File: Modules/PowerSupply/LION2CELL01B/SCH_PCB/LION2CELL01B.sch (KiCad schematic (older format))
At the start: 93 parts, among them J1 JUMP_4X2, J10 JUMP_2x1, J11 JUMP_2x1, J12 JUMP_2x1, J13 JUMP_4X2, J2 JUMP_2x1, J3 JUMP_2x1, J4 JUMP_2x1, J5 JUMP_2x1, J6 JUMP_2x1, J7 JUMP_4X2, J8 CONN1_1, J9 CONN1_1, P1 _, P2 _, P3 _, P4 _, Q1 IRLML6244, Q2 MMBF170LT1G, Q3 MMBF170LT1G, Q4 BSS83P, SW1 SW_PUSH, U1 BQ29209, U2 BQ24103, U3 BQ34Z100, U4 SN74HC164D

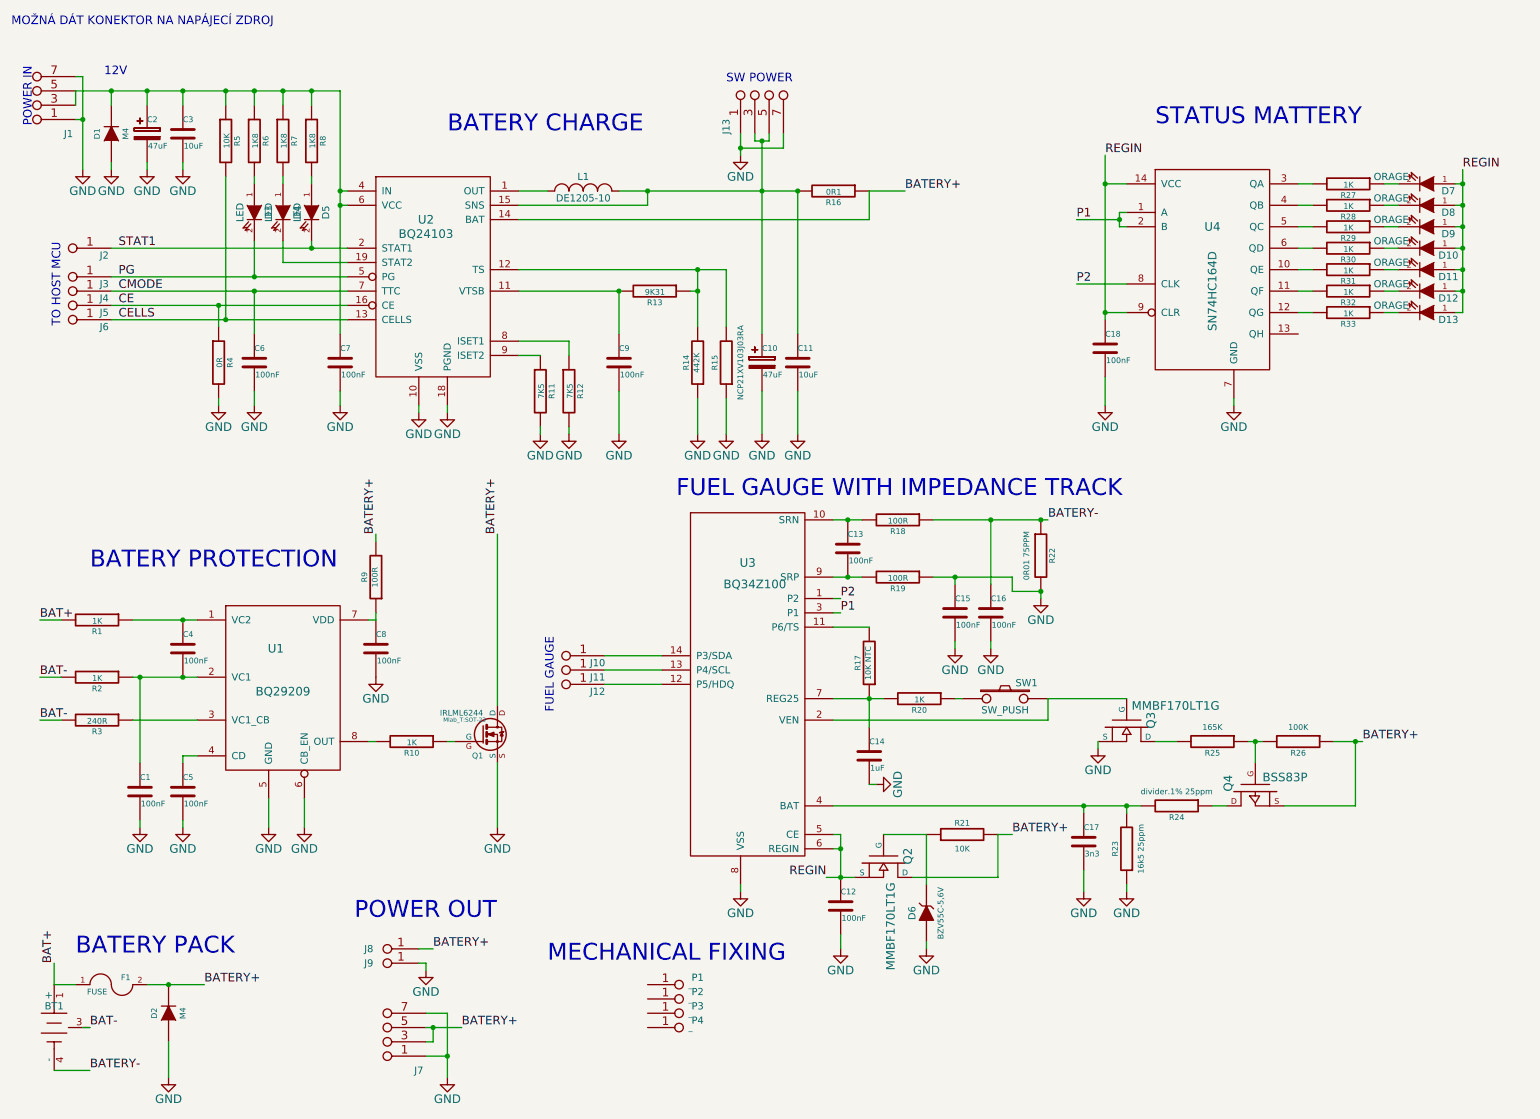
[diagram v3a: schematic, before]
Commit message: Uprava popisku a vedeni spoju ve schema.
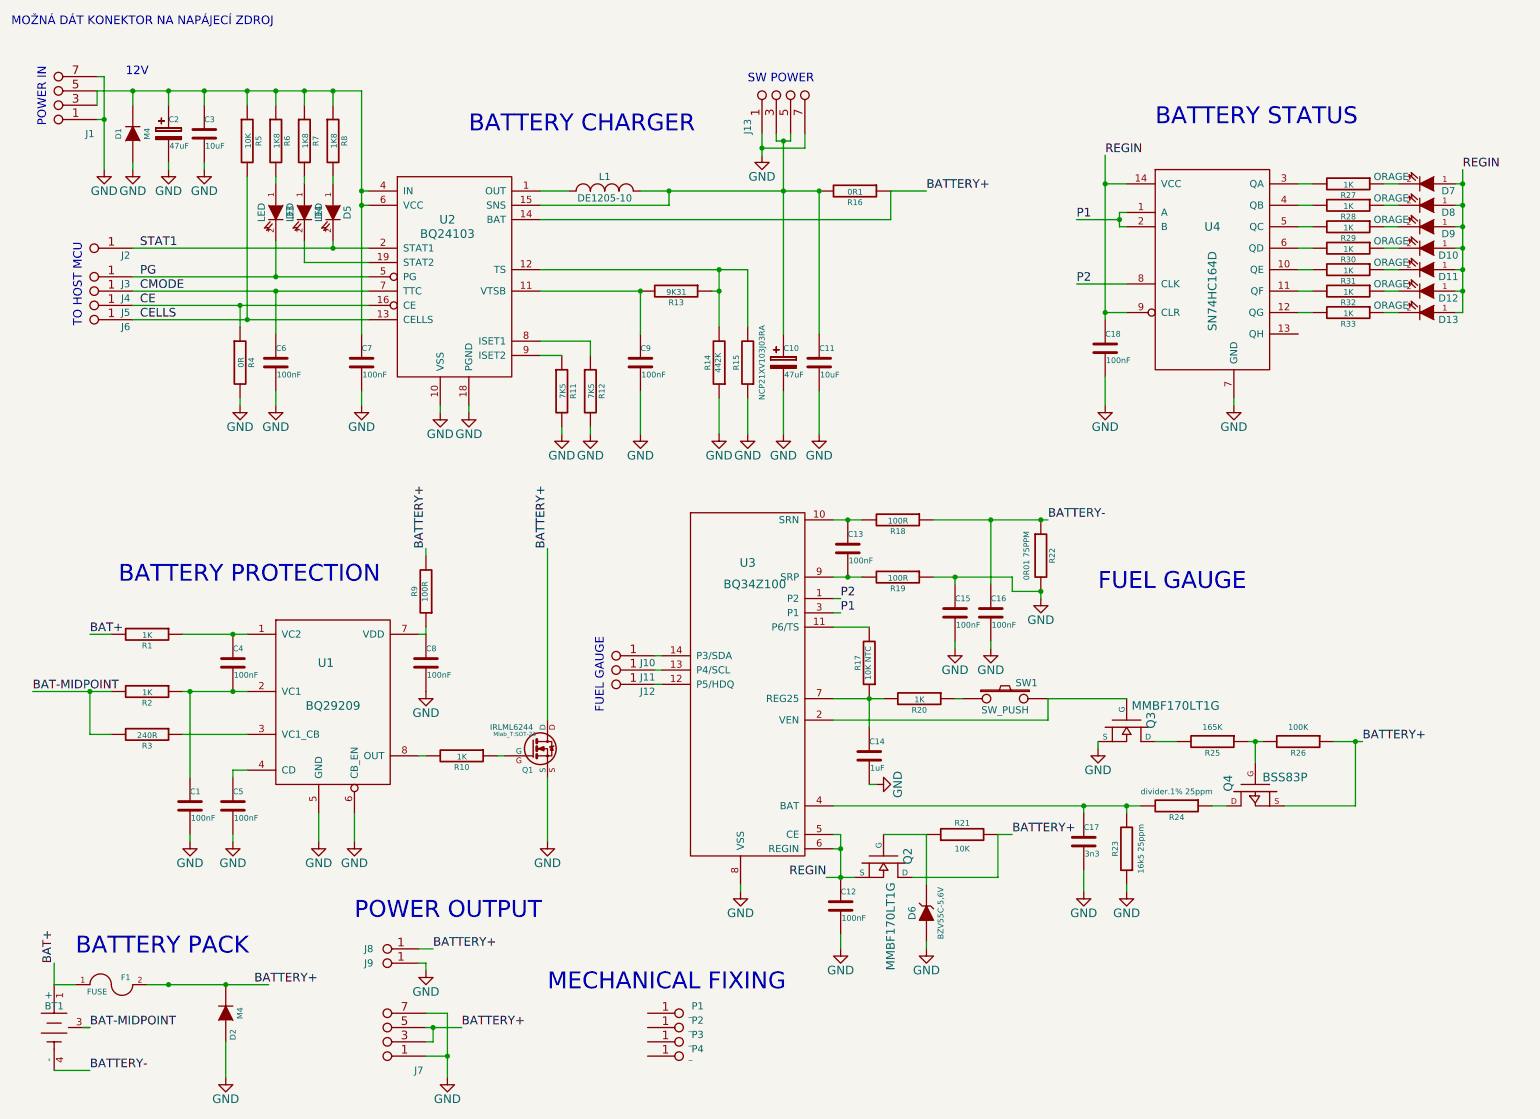
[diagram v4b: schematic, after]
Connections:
- net BAT- renamed BAT-MIDPOINT
- net BATERY+ renamed BATTERY+
- net BATERY- renamed BATTERY-
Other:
- note added: "BATTERY CHARGER"
- note added: "BATTERY PACK"
- note added: "BATTERY PROTECTION"
- note added: "BATTERY STATUS"
- note added: "POWER OUTPUT"
- note removed: "BATERY CHARGE"
- note removed: "BATERY PACK"
- note removed: "BATERY PROTECTION"
- note removed: "FUEL GAUGE WITH IMPEDANCE TRACK"
- note removed: "POWER OUT"
- note removed: "STATUS MATTERY"
- moved on the sheet: C1, C10, C11, C2, C3, C4, C5, C6, C7, C8, C9, D1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

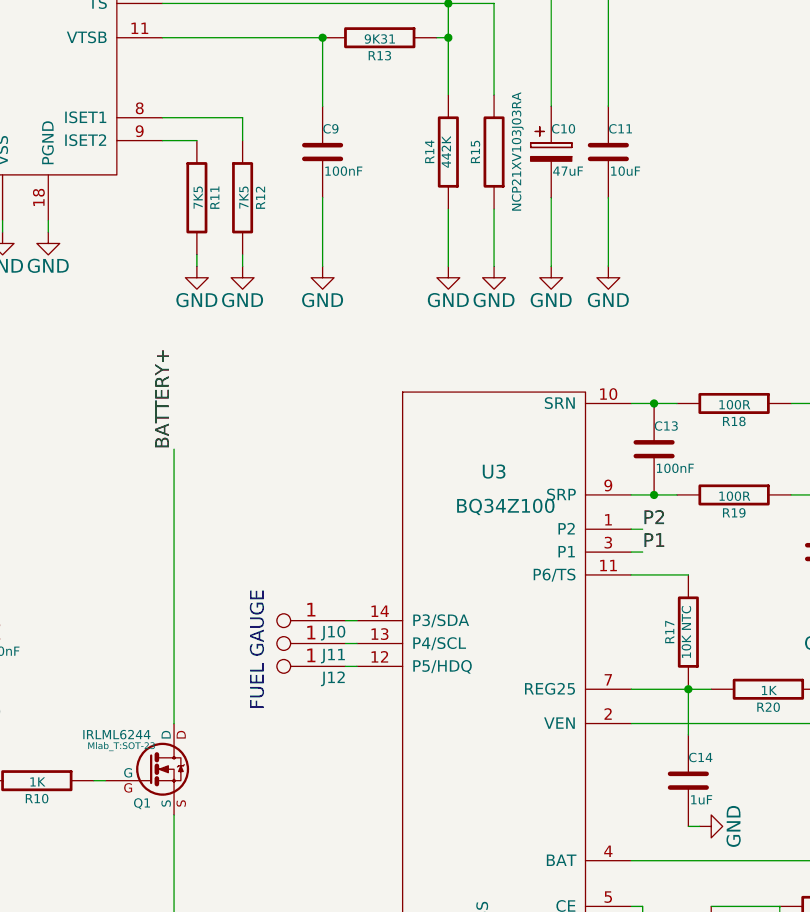
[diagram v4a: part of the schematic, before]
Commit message: 
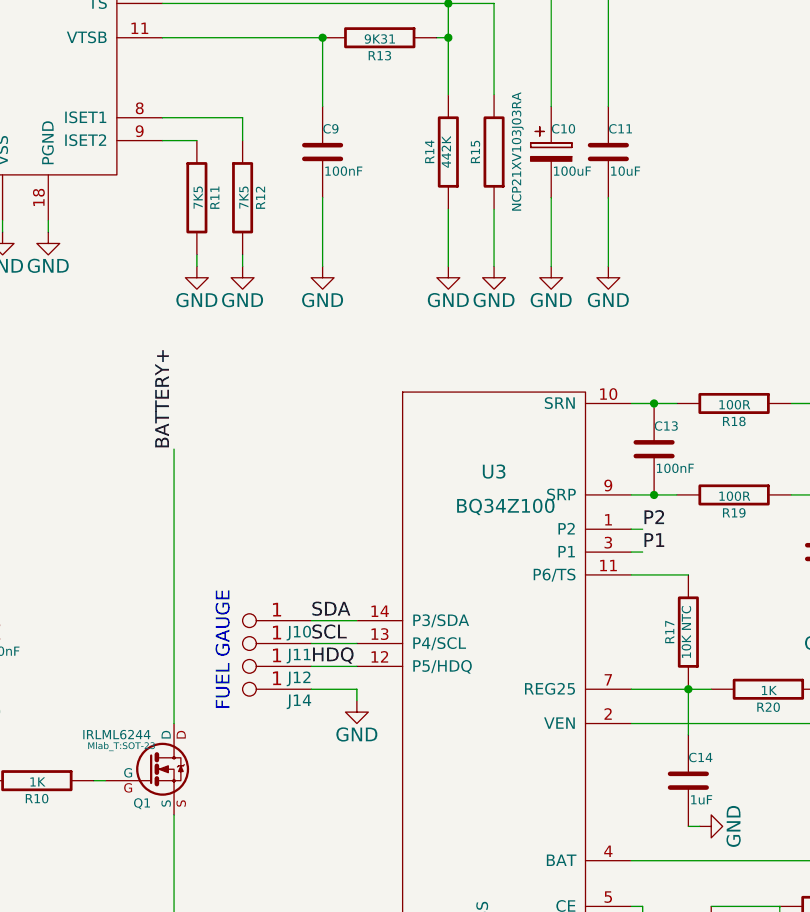
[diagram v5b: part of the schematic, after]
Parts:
- added J14: JUMP_2x1, Mlab_Pin_Headers:Straight_1x02, symbol JUMP_2x1
- C10: value 47uF -> 100uF; footprint Mlab_C:TantalC_SizeC_Reflow -> Mlab_C:TantalC_SizeD_Reflow
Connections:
- net GND: now also J14.1, J14.2 (1)
- net SDA: now reaches J10.1, J10.2 (1), U3.14 (P3/SDA)
- net HDQ: now reaches J12.1, J12.2 (1), U3.12 (P5/HDQ)
- net SCL: now reaches J11.1, J11.2 (1), U3.13 (P4/SCL)
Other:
- moved on the sheet: J10, J11, J12
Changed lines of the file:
@@
 LIBS:contrib
 LIBS:valves
+LIBS:ADC-DAC
+LIBS:asp-134604-01_(fmc)
+LIBS:clock
+LIBS:header
+LIBS:Jumpers
+LIBS:konektory
+LIBS:mechanical
+LIBS:MLAB_D
+LIBS:MLAB_IO
+LIBS:MLAB_Jumpers
+LIBS:OpAmp
+LIBS:sata7-67491-1030
+LIBS:MLAB_BATERY
+LIBS:MLAB_T
 LIBS:LION2CELL01B-cache
 EELAYER 25 0
@@
 L JUMP_2x1 J10
 U 1 1 5532725C
-P 4500 4500
-F 0 "J10" H 4150 4700 50  0000 C CNN
-F 1 "JUMP_2x1" V 4500 4650 40  0001 C CNN
-F 2 "Mlab_Pin_Headers:Straight_1x02" H 4500 4500 60  0001 C CNN
-F 3 "" H 4500 4500 60  0000 C CNN
-	1    4500 4500
+P 4350 4500
+F 0 "J10" H 4000 4700 50  0000 C CNN
+F 1 "JUMP_2x1" V 4350 4650 40  0001 C CNN
+F 2 "Mlab_Pin_Headers:Straight_1x02" H 4350 4500 60  0001 C CNN
+F 3 "" H 4350 4500 60  0000 C CNN
+	1    4350 4500
 	-1   0    0    1
 $EndComp
@@
 P 5800 2600
 F 0 "C10" H 5800 2700 40  0000 L CNN
-F 1 "47uF" H 5806 2515 40  0000 L CNN
-F 2 "Mlab_C:TantalC_SizeC_Reflow" H 5838 2450 30  0001 C CNN
+F 1 "100uF" H 5806 2515 40  0000 L CNN
+F 2 "Mlab_C:TantalC_SizeD_Reflow" H 5838 2450 30  0001 C CNN
 F 3 "" H 5800 2600 60  0000 C CNN
 	1    5800 2600
@@
 L JUMP_2x1 J11
 U 1 1 5535C6AB
-P 4500 4600
-F 0 "J11" H 4150 4800 50  0000 C CNN
-F 1 "JUMP_2x1" V 4500 4750 40  0001 C CNN
-F 2 "Mlab_Pin_Headers:Straight_1x02" H 4500 4600 60  0001 C CNN
-F 3 "" H 4500 4600 60  0000 C CNN
-	1    4500 4600
+P 4350 4600
+F 0 "J11" H 4000 4800 50  0000 C CNN
+F 1 "JUMP_2x1" V 4350 4750 40  0001 C CNN
+F 2 "Mlab_Pin_Headers:Straight_1x02" H 4350 4600 60  0001 C CNN
+F 3 "" H 4350 4600 60  0000 C CNN
+	1    4350 4600
 	-1   0    0    1
 $EndComp
@@
 L JUMP_2x1 J12
 U 1 1 5535C723
-P 4500 4700
-F 0 "J12" H 4150 4900 50  0000 C CNN
-F 1 "JUMP_2x1" V 4500 4850 40  0001 C CNN
-F 2 "Mlab_Pin_Headers:Straight_1x02" H 4500 4700 60  0001 C CNN
-F 3 "" H 4500 4700 60  0000 C CNN
-	1    4500 4700
+P 4350 4700
+F 0 "J12" H 4000 4900 50  0000 C CNN
+F 1 "JUMP_2x1" V 4350 4850 40  0001 C CNN
+F 2 "Mlab_Pin_Headers:Straight_1x02" H 4350 4700 60  0001 C CNN
+F 3 "" H 4350 4700 60  0000 C CNN
+	1    4350 4700
 	-1   0    0    1
 $EndComp
@@
 Wire Wire Line
 	5500 6300 5500 6250
-Text Notes 4550 5050 1    60   ~ 0
+Text Notes 4400 5050 1    60   ~ 0
 FUEL GAUGE
 Connection ~ 4800 2100
@@
 Connection ~ 1900 6950
 Wire Wire Line
-	4950 4650 4900 4650
-Wire Wire Line
-	4950 4750 4900 4750
-Wire Wire Line
-	4900 4850 4950 4850
+	4750 4650 4950 4650
+Wire Wire Line
+	4750 4750 4950 4750
+Wire Wire Line
+	4750 4850 4950 4850
 Wire Wire Line
 	950  5200 950  4900
 Connection ~ 950  4900
+$Comp
+L JUMP_2x1 J14
+U 1 1 55365343
+P 4350 4800
+F 0 "J14" H 4000 5000 50  0000 C CNN
+F 1 "JUMP_2x1" V 4350 4950 40  0001 C CNN
+F 2 "Mlab_Pin_Headers:Straight_1x02" H 4350 4800 60  0001 C CNN
+F 3 "" H 4350 4800 60  0000 C CNN
+	1    4350 4800
+	-1   0    0    1
+$EndComp
+$Comp
+L GND #PWR039
+U 1 1 553655F1
+P 4950 5000
+F 0 "#PWR039" H 4950 4750 60  0001 C CNN
+F 1 "GND" H 4950 4850 60  0000 C CNN
+F 2 "" H 4950 5000 60  0000 C CNN
+F 3 "" H 4950 5000 60  0000 C CNN
+	1    4950 5000
+	1    0    0    -1
+$EndComp
+Wire Wire Line
+	4750 4950 4950 4950
+Wire Wire Line
+	4950 4950 4950 5000
+Text Label 4750 4650 0    60   ~ 0
+SDA
+Text Label 4750 4750 0    60   ~ 0
+SCL
+Text Label 4750 4850 0    60   ~ 0
+HDQ
 $EndSCHEMATC

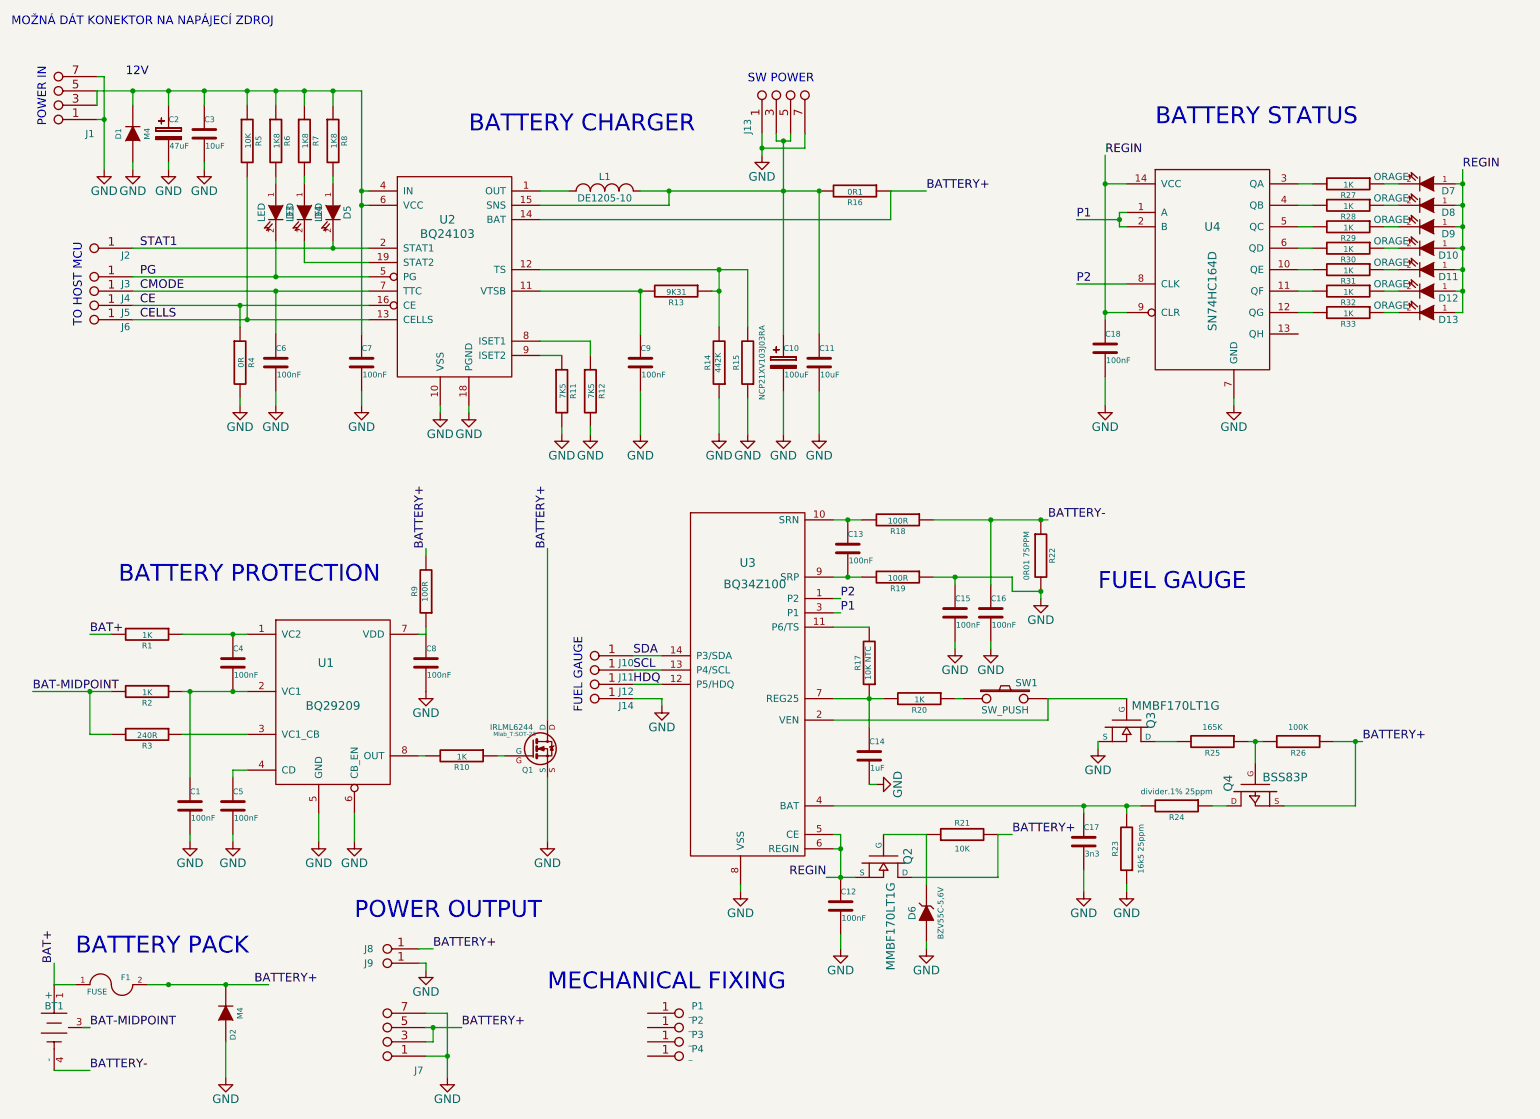
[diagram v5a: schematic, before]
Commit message: 
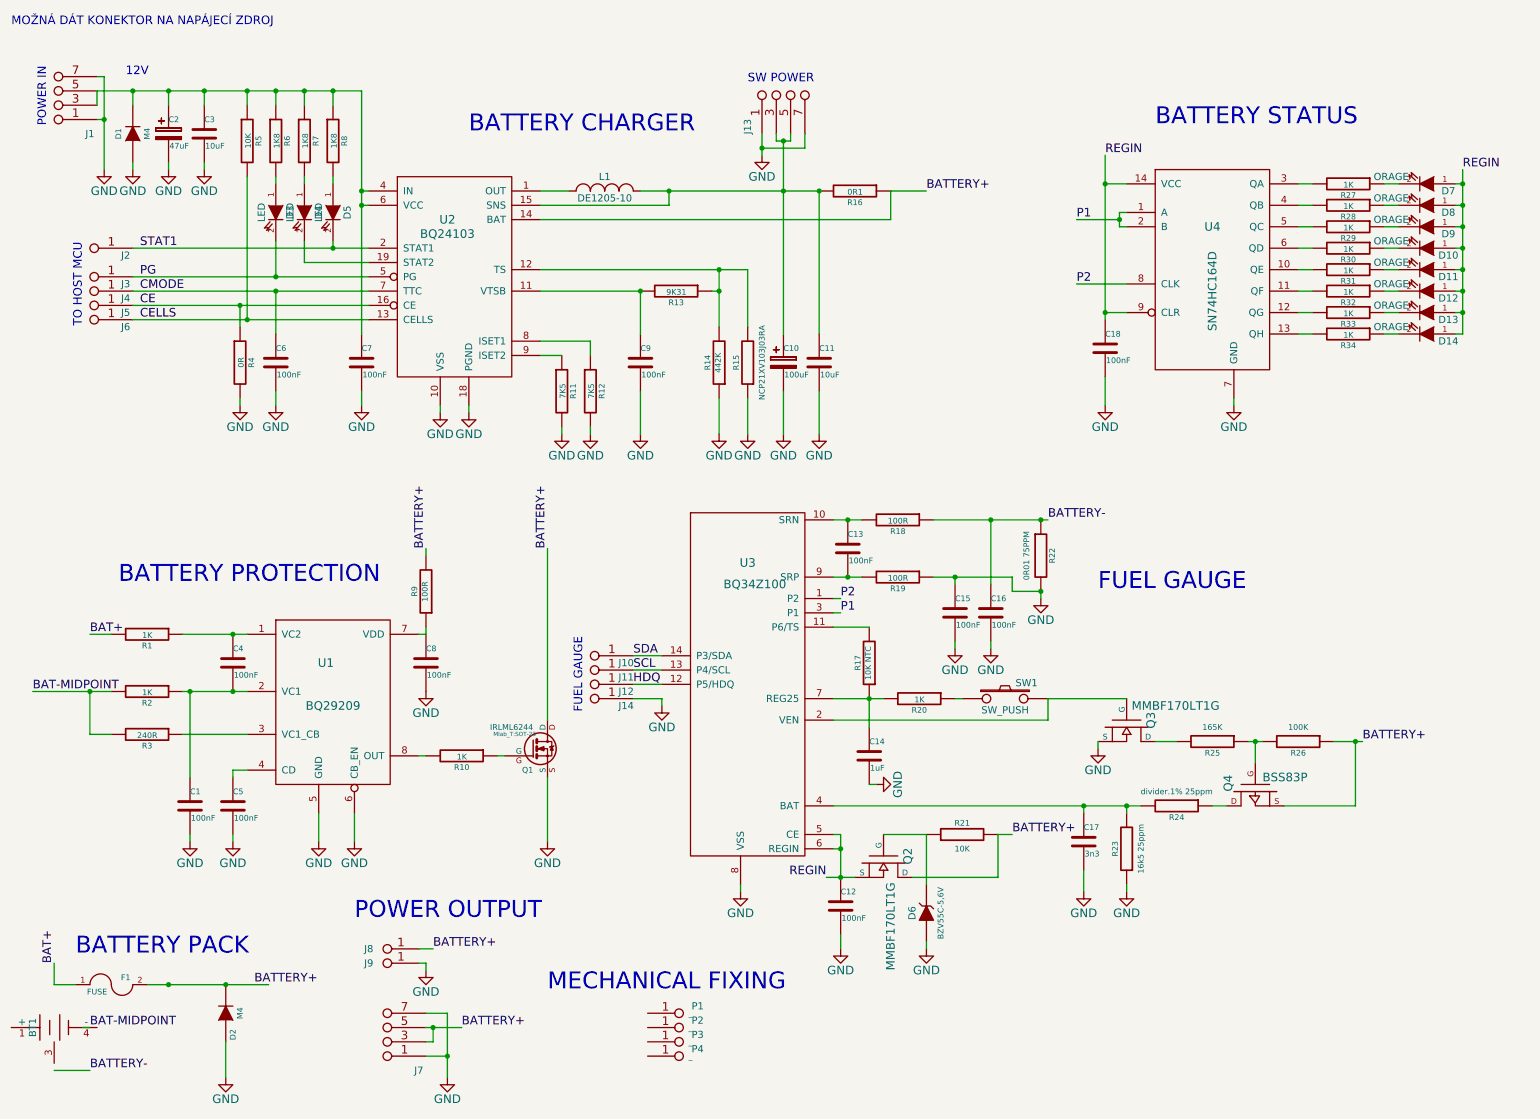
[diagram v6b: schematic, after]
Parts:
- added D14: ORAGE, Mlab_D:LED_1206, symbol LED
- added R34: 1K, Mlab_R:SMD-0805, symbol R
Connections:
- net BAT+: no longer BT1.1 (+)
- net BAT-MIDPOINT: no longer BT1.2, BT1.3
- net BATTERY-: no longer BT1.4 (-)
- net REGIN: now also D14.1 (A)
- net at U4.13 (QH): now also R34.2
- new net: BT1.2, BT1.3
- new net: D14.2 (K), R34.1
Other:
- moved on the sheet: BT1
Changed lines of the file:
@@
 F 3 "" H 2300 7600 60  0000 C CNN
 	1    700  7250
-	0    -1   1    0
+	1    0    0    -1
 $EndComp
 $Comp
@@
 	10500 2250 10550 2250
 Wire Wire Line
-	10550 2250 10550 1250
+	10550 1250 10550 2400
 Wire Wire Line
 	10500 1350 10550 1350
@@
 Text Label 4750 4850 0    60   ~ 0
 HDQ
+$Comp
+L R R34
+U 1 1 5547B85D
+P 9750 2400
+F 0 "R34" V 9830 2400 40  0000 C CNN
+F 1 "1K" V 9757 2401 40  0000 C CNN
+F 2 "Mlab_R:SMD-0805" V 9680 2400 30  0001 C CNN
+F 3 "" H 9750 2400 30  0000 C CNN
+	1    9750 2400
+	0    1    1    0
+$EndComp
+$Comp
+L LED D14
+U 1 1 5547B9F6
+P 10300 2400
+F 0 "D14" H 10150 2450 50  0000 C CNN
+F 1 "ORAGE" H 10550 2350 50  0000 C CNN
+F 2 "Mlab_D:LED_1206" H 10300 2400 60  0001 C CNN
+F 3 "" H 10300 2400 60  0000 C CNN
+	1    10300 2400
+	-1   0    0    1
+$EndComp
+Wire Wire Line
+	10550 2400 10500 2400
+Connection ~ 10550 2250
+Wire Wire Line
+	10000 2400 10100 2400
+Wire Wire Line
+	9500 2400 9400 2400
 $EndSCHEMATC
